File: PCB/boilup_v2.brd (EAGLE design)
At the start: 45.6 x 54.7 mm, 36 parts, among them IC1 THS4211, J1 USB-MICROB, U1 STM32F0_LQFP64, U2 SPX3819-3.3

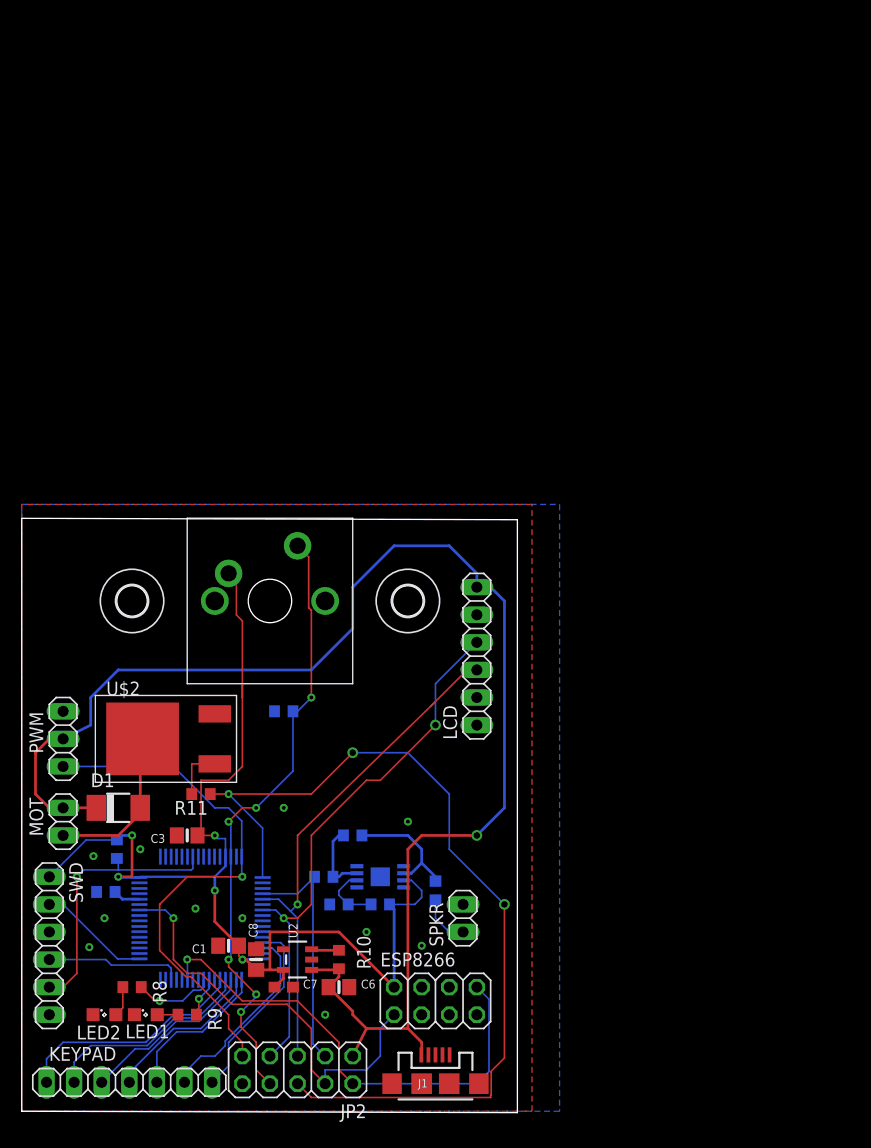
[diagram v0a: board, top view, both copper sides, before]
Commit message: Added V2 brd layout
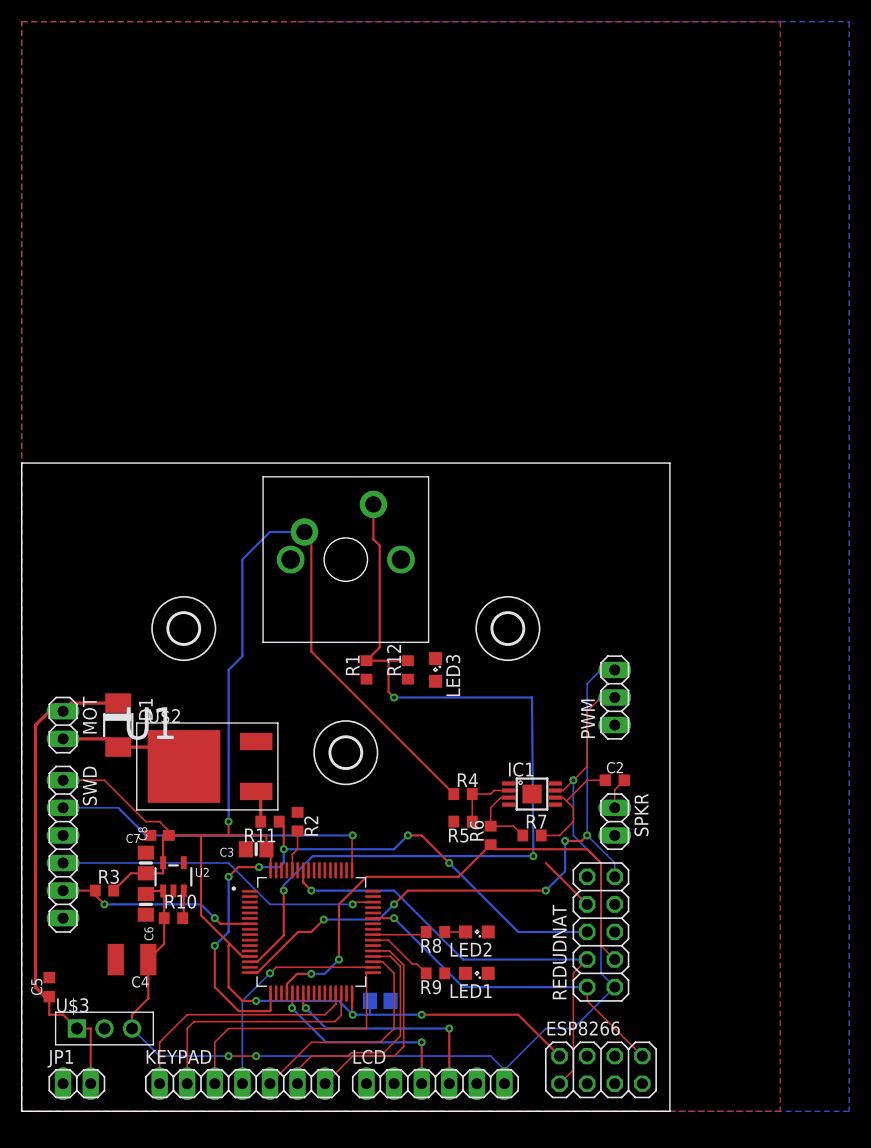
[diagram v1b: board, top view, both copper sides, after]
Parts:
- removed J1: USB-MICROB, SparkFun-Connectors:USB-MICROB
- removed JP2: (no value), pinhead:2X05
- added C4: 100uF, resistor:C1210K
- added C5: 10uF, resistor:C0603K
- added H3: MOUNT-HOLE2.8, holes:2,8
- added JP1: (no value), pinhead:1X02
- added LED3: (no value), led:SML0805
- added R12: (no value), resistor:R0603
- added REDUDNAT: (no value), pinhead:2X05
- added U$3: TPSM842, smarttle:TO-220
- moved PWM 50.9 mm to (54.6, 38.1), turned to 90 degrees
- moved LCD 39.6 mm to (38.1, 2.54), turned to 0 degrees
- moved LED2 35.1 mm to (41.9, 16.5), turned to 180 degrees
- moved H2 34.7 mm to (44.8, 44.5)
- moved LED1 30.7 mm to (41.9, 12.7), turned to 180 degrees
- moved R8 28.4 mm to (38.1, 16.5), turned to 180 degrees
- moved R9 23.2 mm to (38.1, 12.7), turned to 180 degrees
- moved H1 20.8 mm to (14.9, 44.5)
- moved C2 19.4 mm to (54.6, 30.5), flipped to the top, turned to 0 degrees
- moved C6 19.3 mm to (11.4, 19.1), turned to 270 degrees
- moved R2 18.8 mm to (25.4, 26.7), flipped to the top, turned to 270 degrees
- moved C7 18.1 mm to (12.7, 25.4), turned to 180 degrees
- moved SPKR 16.6 mm to (54.6, 26.7), turned to 270 degrees
- moved ESP8266 16.5 mm to (53.3, 3.81)
- moved R7 16.5 mm to (47.0, 25.4), flipped to the top, turned to 0 degrees
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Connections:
- removed net D+: J1.D+
- removed net D-: J1.D-
- new net +12V: C5.1, D1.C, JP1.2, MOT.1, U$3.P$1
- new net N$5: LED3.A, R12.1
- net +3V3: no longer IC1.7
- net +5V: now also C4.1, IC1.7, REDUDNAT.1, U$3.P$3; no longer D1.C, J1.VBUS, JP2.1, MOT.1
- net DAC: now also REDUDNAT.3; no longer JP2.3
- net GND: now also C4.2, C5.2, JP1.1, LED3.C, REDUDNAT.10, U$3.P$2; no longer J1.GND, J1.MT1, J1.MT2, JP2.10
- net MOSI: no longer JP2.7
- net PUSH_BUTT: now also R12.2, REDUDNAT.8; no longer JP2.8
- net SCK: no longer JP2.5
- net TIM2_CH3: now also REDUDNAT.9; no longer JP2.9
- net TIM2_CH4: now also REDUDNAT.6; no longer JP2.6
- net USART_RX: now also REDUDNAT.2; no longer JP2.2
- net USART_TX: now also REDUDNAT.4; no longer JP2.4
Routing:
- net +12V: track 0.00 -> 45.3 mm
- net +3V3: track 106.3 -> 150.8 mm, vias 5 -> 4
- net +5V: track 132.9 -> 99.1 mm, vias 1 -> 3
- net PUSH_BUTT: track 57.1 -> 88.1 mm, vias 6 -> 3
- net MOSI: track 50.2 -> 20.5 mm
- net SCK: track 47.2 -> 18.4 mm, vias 1 -> 2
- net DAC: track 22.3 -> 48.2 mm, vias 0 -> 2
- net TIM2_CH4: track 83.1 -> 60.1 mm, vias 3 -> 6
- net SWCLK: track 10.4 -> 31.0 mm, vias 0 -> 1
- net SWDIO: track 12.6 -> 30.2 mm, vias 0 -> 1
- net USART_RX: track 44.6 -> 30.8 mm
- net TIM2_CH3: track 49.7 -> 59.8 mm, vias 1 -> 5
- net ROW3: track 14.1 -> 24.0 mm
- net NRST: track 25.1 -> 18.7 mm, vias 1 -> 2
- net ROW4: track 15.0 -> 20.9 mm, vias 0 -> 1
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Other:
- board size 45.6 x 54.7 mm -> 59.7 x 59.7 mm

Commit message: replaced speaker circuit, redid board layout. V2 is active development version
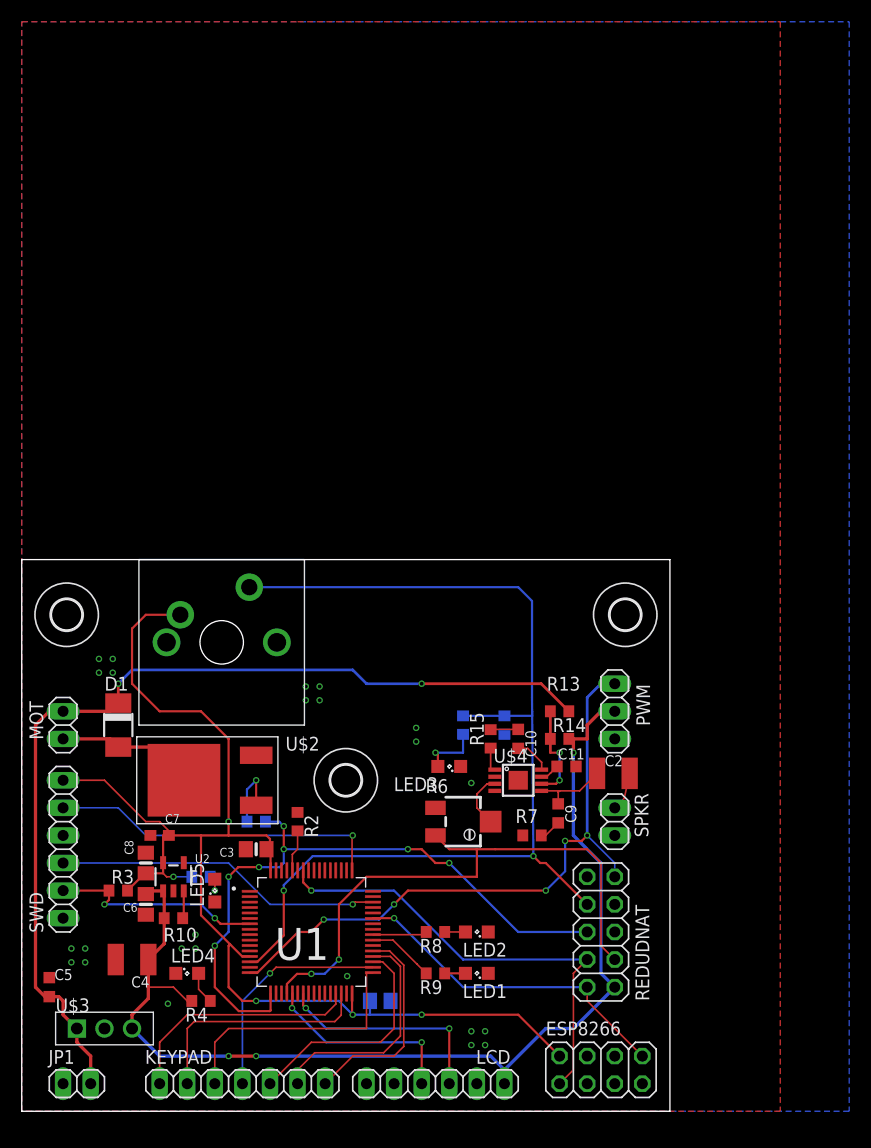
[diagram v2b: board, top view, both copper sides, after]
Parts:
- removed IC1: THS4211, texas:S-PDSO-G08
- added C10, C11, C9: 0.05uF, resistor:C0603K
- added LED4, LED5: (no value), led:SML0805
- added R13, R14: 0, resistor:R0603
- added R15: 10, resistor:R0603
- added U$4: LM386, smarttle:S-PDSO-G08
- C2: device resistor:C0603K -> resistor:C1210K
- R6: device resistor:R0603 -> resistor:RTRIM3224X
- R7: value (none) -> 10
- moved H1 40.7 mm to (55.6, 45.7)
- moved H2 40.6 mm to (4.14, 45.7)
- moved R4 30.7 mm to (16.5, 10.2), turned to 180 degrees
- moved R5 24.7 mm to (16.5, 21.6), flipped to the bottom, turned to 0 degrees
- moved U$1 13.7 mm to (18.4, 43.2)
- moved R1 13.7 mm to (44.5, 35.6), flipped to the bottom
- moved LED3 8.98 mm to (39.4, 31.8), turned to 180 degrees
- moved R12 7.18 mm to (40.6, 35.6), flipped to the bottom
- moved R6 2.84 mm to (40.6, 26.7), turned to 270 degrees
- moved H3 2.54 mm to (29.8, 30.5)
- moved PWM 1.27 mm to (54.6, 36.8)
- moved R3 1.27 mm to (8.89, 20.3)
- moved R11 1.27 mm to (21.6, 26.7), flipped to the bottom, turned to 0 degrees
- moved U$2 1.27 mm to (21.6, 30.5)
- moved C2 0.65 mm to (54.5, 31.1)
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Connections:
- removed net AMP: IC1.3, R6.2, R7.1
- removed net N$17: C2.1, IC1.6, R7.2
- new net N$10: R15.1, U$4.1
- new net N$11: C10.2, U$4.8
- new net N$12: C10.1, R15.2
- new net N$13: C11.1, U$4.7
- new net N$14: LED5.A, R5.1
- new net N$6: C9.2, R7.1
- new net N$8: C2.1, C9.1, U$4.5
- new net N$9: R6.2, U$4.3
- new net OPAMPSUPPLY: R13.2, R14.1, U$4.6
- net +12V: now also R13.1
- net +3V3: now also R5.2; no longer R4.1
- net +5V: now also R14.2, R4.2; no longer IC1.7
- net DAC: now also R6.3; no longer R6.1
- net GND: now also C11.2, LED4.C, LED5.C, R6.1, R7.2, U$4.2, U$4.4; no longer IC1.4, R5.2
- net N$7: now also LED4.A, R4.1; no longer IC1.2, R4.2, R5.1
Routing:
- net +12V: track 45.3 -> 89.7 mm, vias 0 -> 2
- net +3V3: track 150.8 -> 119.5 mm, vias 4 -> 5
- net N$17: track 11.2 -> 0.00 mm
- net OPAMPSUPPLY: track 0.00 -> 8.99 mm, vias 0 -> 2
- net PUSH_BUTT: track 88.1 -> 96.5 mm, vias 3 -> 2
- net AMP: track 7.05 -> 0.00 mm
- net N$8: track 0.00 -> 7.02 mm
- net N$5: track 0.00 -> 5.59 mm, vias 0 -> 1
- net DAC: track 48.2 -> 53.7 mm
- net N$9: track 0.00 -> 5.11 mm
- net N$4: track 2.95 -> 6.46 mm, vias 0 -> 1
- net N$11: track 0.00 -> 3.37 mm
- net N$7: track 6.02 -> 2.98 mm
- net N$12: track 0.00 -> 2.55 mm
- net N$14: track 0.00 -> 2.49 mm, vias 0 -> 1
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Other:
- board size 59.7 x 59.7 mm -> 59.7 x 50.8 mm

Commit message: More small updates. check v2
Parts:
- renumbered LED3 to BUTTON, LED4 to 5V, LED5 to 3V3, REDUDNAT to REDUNDANT
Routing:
- net +5V: track 101.5 -> 100.7 mm
- net DAC: track 53.7 -> 54.2 mm
